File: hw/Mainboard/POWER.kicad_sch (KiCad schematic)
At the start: 54 parts, among them J10 5V PWR, J11 9V POWER, J18 PET POWER, J7 9V POWER, U10 XL1509-5.0E1, U13 AMS1117-3.3, U15 LM317AG-TN3-R, U17 LM1117-1.2

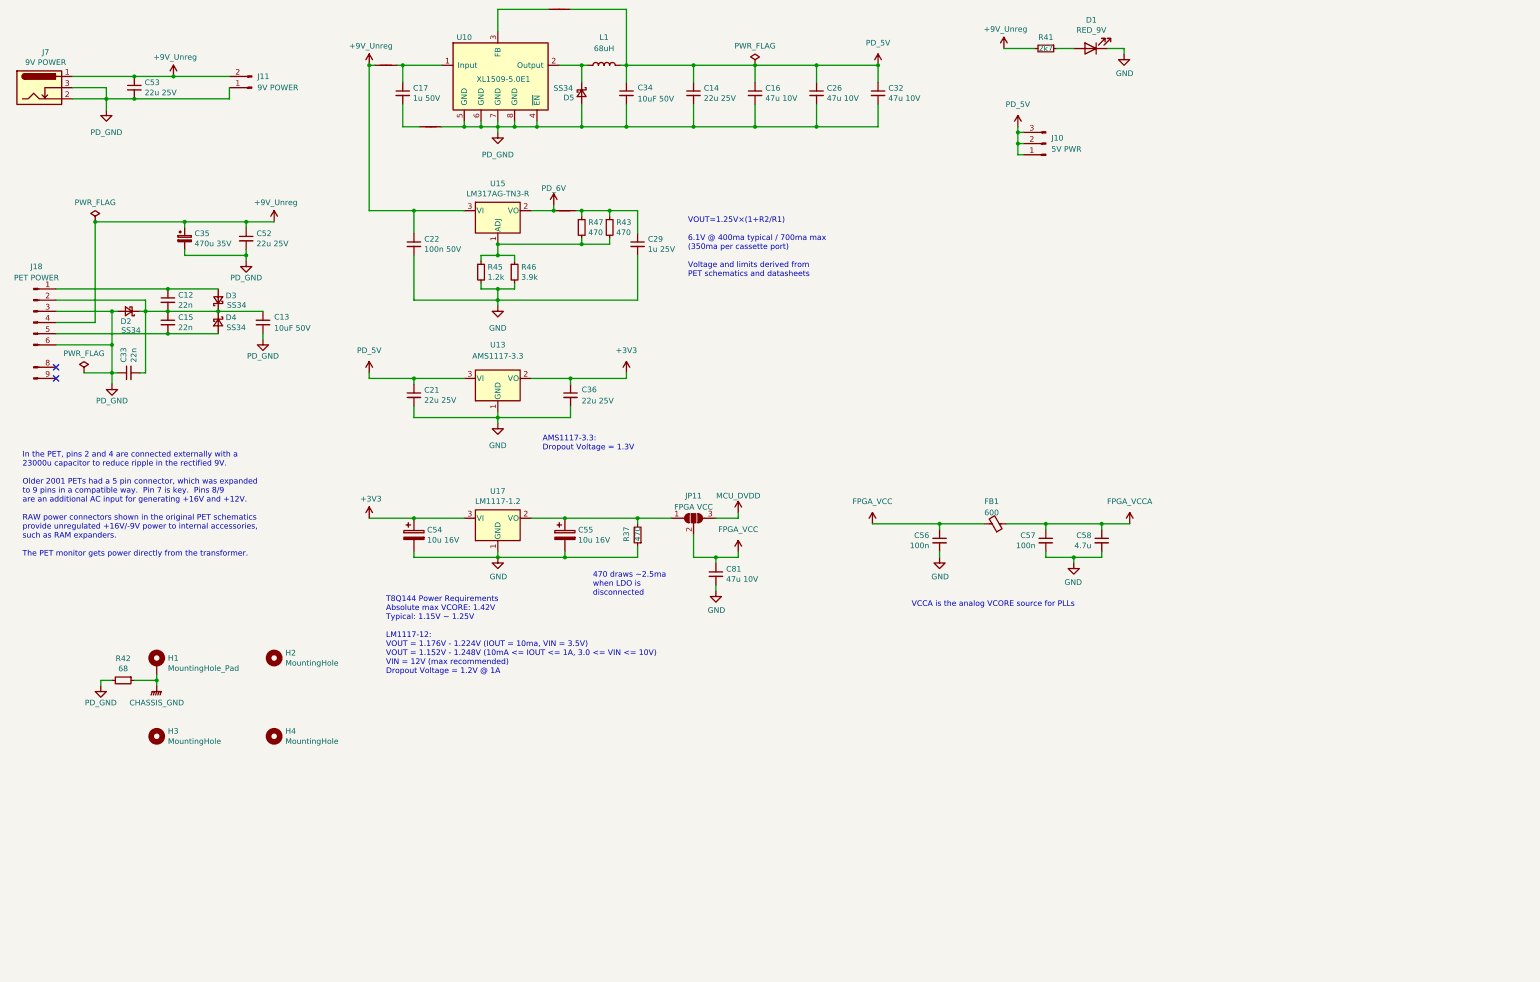
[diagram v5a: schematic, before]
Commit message: hw: larger schematic pages, routed w/netties
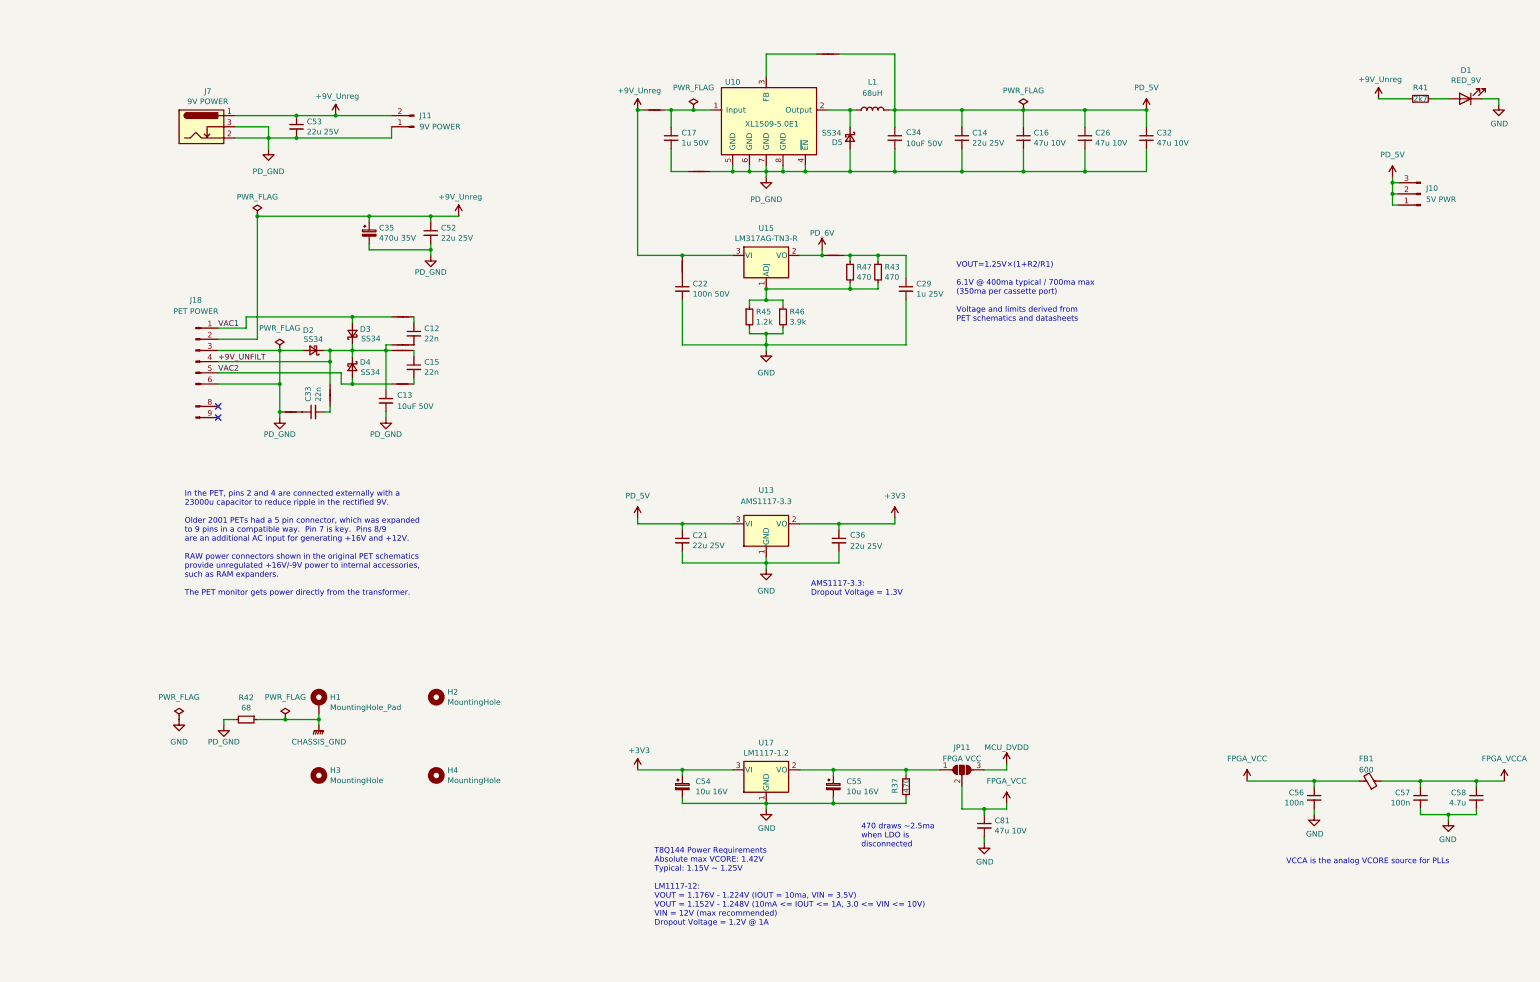
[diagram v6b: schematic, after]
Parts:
- added NT25, NT26, NT27, NT28, NT29, NT30, NT31: +9V, PET:NetTie-2_SMD_Pad_1.6_to_0.4mm, symbol Device:NetTie_2
- C54, C55: symbol T8Dev-rescue:CP-Device -> Device:C_Polarized_Small
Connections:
- net +9V_Unreg: now also J18.2 (Pin_2), NT25.1; no longer C22.1, J18.4 (Pin_4)
- net PD_GND: now also NT30.1; no longer C33.1
- net VAC1: now reaches D3.2 (A), J18.1 (Pin_1)
- net VAC1: now also NT26.1; no longer C12.1
- net +9V_UNFILT: now reaches C13.1, D2.1 (K), D3.1 (K), D4.1 (K)
- net +9V_UNFILT: now also J18.4 (Pin_4), NT27.1, NT29.1, NT31.1; no longer C12.2, C15.1, C33.2, J18.2 (Pin_2)
- net VAC2: now reaches D4.2 (A), J18.5 (Pin_5)
- net VAC2: now also NT28.1; no longer C15.2
- new net: C12.1, NT26.2
- new net: C12.2, NT31.2
- new net: C15.1, NT27.2
- new net: C15.2, NT28.2
- new net: C33.1, NT30.2
- new net: C33.2, NT29.2
- new net: C22.1, NT25.2
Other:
- moved on the sheet: C12, C13, C14, C15, C16, C17, C21, C22, C26, C29, C32, C33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

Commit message: hw: wip
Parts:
- added PT4: PowerTie_2, PET:NetTie-2_SMD_Pad_1.6_to_0.4mm, symbol PET:PowerTie_2
- J18: symbol PET:PET_Power_01x09_Male -> Retrocomputing:CBM_PET_POWER_01x09_Male_Keyed
- NT1, NT16, NT17, NT2, NT25: symbol Device:NetTie_2 -> PET:PowerTie_2
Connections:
- net GND: no longer C21.2, C36.2, C54.2, C55.2, C81.2, R37.1, U13.1 (GND), U17.1 (GND)
- net PD_GND: now also C21.2, C36.2, C54.2, C55.2, C81.2, U13.1 (GND), U17.1 (GND), PT4.1
- net +3V3 renamed PD_3V3
- net +9V_UNFILT: no longer names the net of C13.1, D2.1 (K), D3.1 (K), D4.1 (K), J18.4 (9V_OUT), NT27.1, NT29.1, NT31.1
- net FPGA_VCC renamed +1V2
- new net: PT4.2, R37.1
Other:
- note added: "+9V_IN"
- note added: "+9V_OUT"
- note added: "GND"
- note added: "Pins 2 and 4 are connected externally with a 23000u capacitor to reduce ripple in the rectified 9V. Older 2001 PETs had a 5 pin connector, which was expanded to 9 pins in a compatible way. Pin 7 is key. Pins 8/9 are an additional AC input for generating +16V and +12V. RAW power connectors shown in the original PET schematics provide unregulated +16V/-9V power to internal accessories, such as RAM 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"
- note added: "T8Q144 Power Requirements Absolute max VCORE: 1.42V Typical: 1.15V ~ 1.25V LM1117-12: VOUT = 1.176V - 1.224V (IOUT = 10ma, VIN = 3.5V) VOUT = 1.152V - 1.248V (10mA <= IOUT <= 1A, 3.0 <= VIN <= 10V) VIN = 12V (max recommended) Dropout Voltage = 1.2V @ 1A MCU_DVDD (RP2040): VOUT = 1.1V at POR, set to 1.2V in firmware IOUT = 100ma max, RP2040 draws ~40ma for FFT @ 1.21V / 150 MHz"
- note removed: "In the PET, pins 2 and 4 are connected externally with a 23000u capacitor to reduce ripple in the rectified 9V. Older 2001 PETs had a 5 pin connector, which was expanded to 9 pins in a compatible way. Pin 7 is key. Pins 8/9 are an additional AC input for generating +16V and +12V. RAW power connectors shown in the original PET schematics provide unregulated +16V/-9V power to internal accessories, 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"
- note removed: "T8Q144 Power Requirements Absolute max VCORE: 1.42V Typical: 1.15V ~ 1.25V LM1117-12: VOUT = 1.176V - 1.224V (IOUT = 10ma, VIN = 3.5V) VOUT = 1.152V - 1.248V (10mA <= IOUT <= 1A, 3.0 <= VIN <= 10V) VIN = 12V (max recommended) Dropout Voltage = 1.2V @ 1A"
- moved on the sheet: C35, C52, C56, C57, C58, D2, FB1, JP11

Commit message: hw: wip
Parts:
- FB1: symbol T8Dev-rescue:Ferrite_Bead_Small-Device -> Device:FerriteBead_Small
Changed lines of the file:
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@@
     (pin "2")
   )
-  (symbol (lib_id "T8Dev-rescue:Ferrite_Bead_Small-Device") (at 284.48 204.47 270) (mirror x) (unit 1)
+  (symbol (lib_id "Device:FerriteBead_Small") (at 284.48 204.47 270) (mirror x) (unit 1)
     (in_bom yes) (on_board yes)
     (property "Reference" "FB1" (id 0) (at 281.94 199.39 90)
@@
       (effects (font (size 1.27 1.27)) hide)
     )
-    (property "Datasheet" "https://datasheet.lcsc.com/lcsc/1811091241_Sunlord-GZ1608D601TF_C1002.pdf" (id 3) (at 284.48 204.47 0)
+    (property "Datasheet" "~" (id 3) (at 284.48 204.47 0)
       (effects (font (size 1.27 1.27)) hide)
     )
@@
     (pin "1")
   )
-  (symbol (lib_name "PD_GND_4") (lib_id "PET:PD_GND") (at 76.2 54.61 0) (unit 1)
+  (symbol (lib_id "PET:PD_GND") (at 76.2 54.61 0) (unit 1)
     (in_bom yes) (on_board yes) (fields_autoplaced)
     (property "Reference" "#PWR0130" (id 0) (at 76.2 60.96 0)
@@
     (pin "2")
   )
-  (symbol (lib_name "PD_5V_1") (lib_id "PET:PD_5V") (at 275.59 45.72 0) (unit 1)
+  (symbol (lib_id "PET:PD_5V") (at 275.59 45.72 0) (unit 1)
     (in_bom yes) (on_board yes) (fields_autoplaced)
     (property "Reference" "#PWR0157" (id 0) (at 275.59 49.53 0)
@@
     (pin "2")
   )
-  (symbol (lib_name "PD_3V3_1") (lib_id "PET:PD_3V3") (at 160.02 194.31 0) (unit 1)
+  (symbol (lib_id "PET:PD_3V3") (at 160.02 194.31 0) (unit 1)
     (in_bom yes) (on_board yes) (fields_autoplaced)
     (property "Reference" "#PWR0222" (id 0) (at 160.02 198.12 0)
@@
     (pin "1")
   )
-  (symbol (lib_name "PD_GND_2") (lib_id "PET:PD_GND") (at 102.87 78.74 0) (unit 1)
+  (symbol (lib_id "PET:PD_GND") (at 102.87 78.74 0) (unit 1)
     (in_bom yes) (on_board yes)
     (property "Reference" "#PWR0132" (id 0) (at 102.87 85.09 0)
@@
     (pin "2")
   )
-  (symbol (lib_name "PD_GND_2") (lib_id "PET:PD_GND") (at 78.74 115.57 0) (unit 1)
+  (symbol (lib_id "PET:PD_GND") (at 78.74 115.57 0) (unit 1)
     (in_bom yes) (on_board yes)
     (property "Reference" "#PWR0116" (id 0) (at 78.74 121.92 0)
@@
     )
   )
-  (symbol (lib_name "PD_GND_2") (lib_id "PET:PD_GND") (at 102.87 115.57 0) (unit 1)
+  (symbol (lib_id "PET:PD_GND") (at 102.87 115.57 0) (unit 1)
     (in_bom yes) (on_board yes)
     (property "Reference" "#PWR0131" (id 0) (at 102.87 121.92 0)
@@
     (pin "2")
   )
-  (symbol (lib_name "PD_GND_3") (lib_id "PET:PD_GND") (at 66.04 185.42 0) (unit 1)
+  (symbol (lib_id "PET:PD_GND") (at 66.04 185.42 0) (unit 1)
     (in_bom yes) (on_board yes)
     (property "Reference" "#PWR0121" (id 0) (at 66.04 191.77 0)
